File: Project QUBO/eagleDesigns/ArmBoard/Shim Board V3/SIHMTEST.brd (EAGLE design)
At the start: 79 x 69 mm, 30 parts, among them IC1 MCP2551/SN, U1 BME280

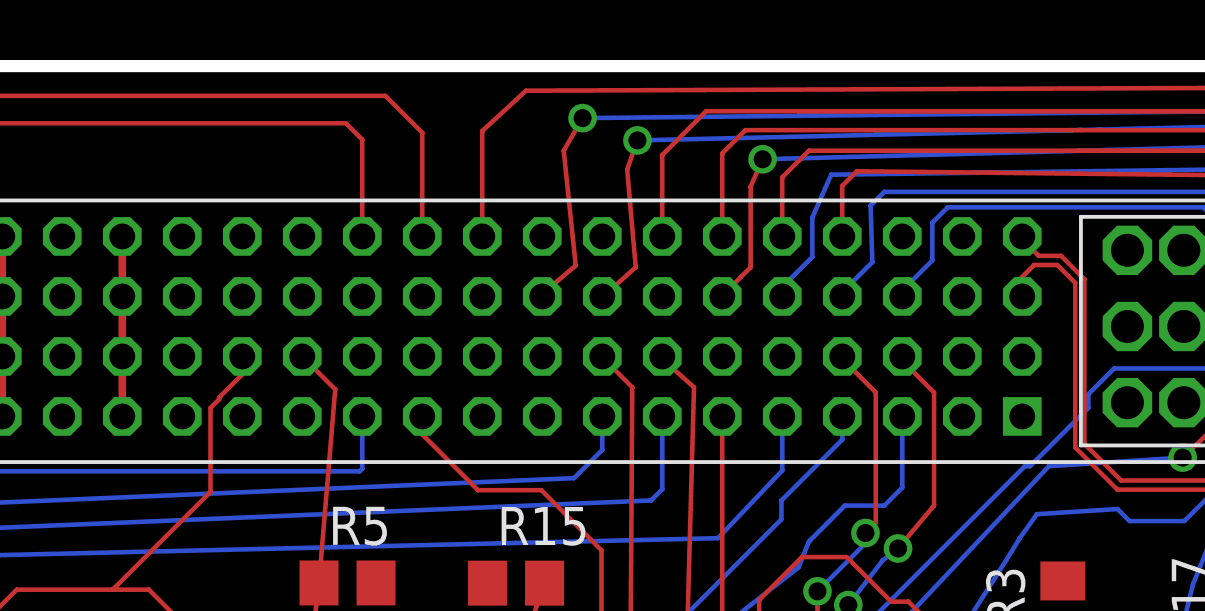
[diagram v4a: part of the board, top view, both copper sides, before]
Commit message: 
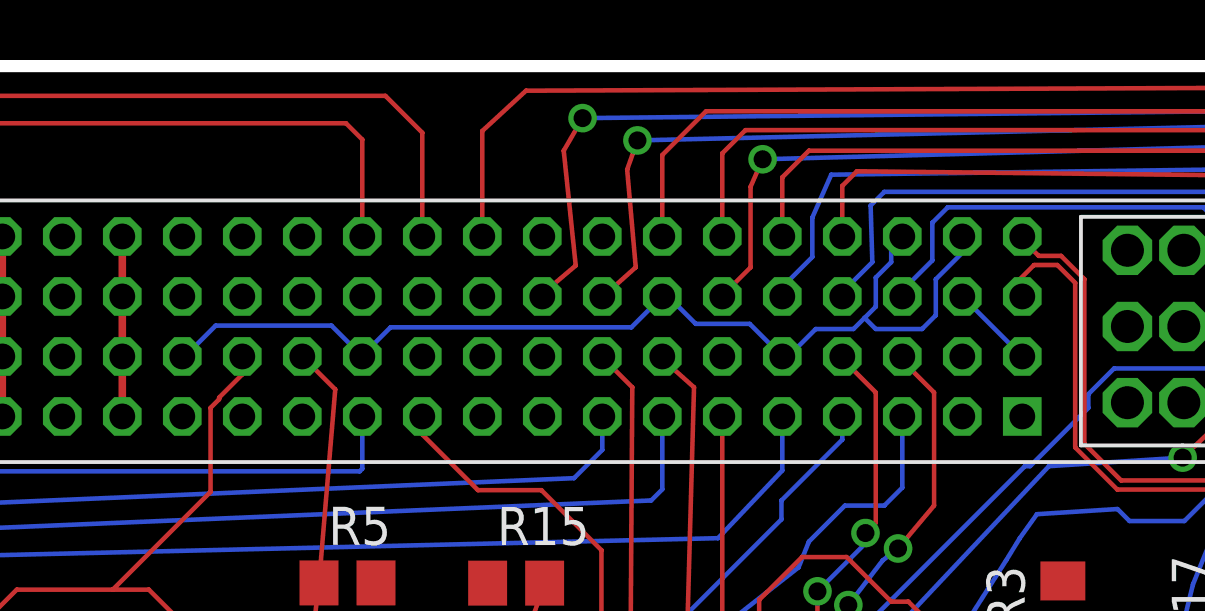
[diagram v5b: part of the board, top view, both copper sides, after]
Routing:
- net DGND: track 35.3 -> 72.8 mm
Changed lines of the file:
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@@
 <wire x1="70.58025" y1="43.94835" x2="64.7446" y2="43.94835" width="0.1524" layer="1"/>
 <wire x1="64.7446" y1="43.94835" x2="64.73825" y2="43.942" width="0.1524" layer="1"/>
-<wire x1="56.2049" y1="63.32125" x2="54.2049" y2="63.32125" width="0" layer="19" extent="1-1"/>
-<wire x1="58.2049" y1="59.32125" x2="56.2049" y2="61.32125" width="0" layer="19" extent="1-1"/>
-<wire x1="50.2049" y1="59.32125" x2="54.2049" y2="63.32125" width="0" layer="19" extent="1-1"/>
-<wire x1="46.2049" y1="61.32125" x2="50.2049" y2="59.32125" width="0" layer="19" extent="1-1"/>
-<wire x1="36.2049" y1="59.32125" x2="46.2049" y2="61.32125" width="0" layer="19" extent="1-1"/>
-<wire x1="30.2049" y1="59.32125" x2="36.2049" y2="59.32125" width="0" layer="19" extent="1-1"/>
+<wire x1="30.2049" y1="59.32125" x2="30.28905" y2="59.32125" width="0.1524" layer="16"/>
+<wire x1="30.28905" y1="59.32125" x2="31.3182" y2="60.3504" width="0.1524" layer="16"/>
+<wire x1="31.3182" y1="60.3504" x2="35.17575" y2="60.3504" width="0.1524" layer="16"/>
+<wire x1="35.17575" y1="60.3504" x2="36.2049" y2="59.32125" width="0.1524" layer="16"/>
+<wire x1="36.2049" y1="59.32125" x2="36.2049" y2="59.35065" width="0.1524" layer="16"/>
+<wire x1="36.2049" y1="59.35065" x2="37.1475" y2="60.29325" width="0.1524" layer="16"/>
+<wire x1="37.1475" y1="60.29325" x2="45.1769" y2="60.29325" width="0.1524" layer="16"/>
+<wire x1="45.1769" y1="60.29325" x2="46.2049" y2="61.32125" width="0.1524" layer="16"/>
+<wire x1="46.2049" y1="61.32125" x2="46.4065" y2="61.32125" width="0.1524" layer="16"/>
+<wire x1="46.4065" y1="61.32125" x2="47.3202" y2="60.40755" width="0.1524" layer="16"/>
+<wire x1="47.3202" y1="60.40755" x2="49.1186" y2="60.40755" width="0.1524" layer="16"/>
+<wire x1="49.1186" y1="60.40755" x2="50.2049" y2="59.32125" width="0.1524" layer="16"/>
+<wire x1="50.2049" y1="59.32125" x2="50.40585" y2="59.32125" width="0.1524" layer="16"/>
+<wire x1="50.40585" y1="59.32125" x2="51.3207" y2="60.2361" width="0.1524" layer="16"/>
+<wire x1="51.3207" y1="60.2361" x2="52.578" y2="60.2361" width="0.1524" layer="16"/>
+<wire x1="52.949475" y1="60.607575" x2="52.578" y2="60.2361" width="0.1524" layer="16"/>
+<wire x1="52.949475" y1="60.607575" x2="53.32095" y2="60.97905" width="0.1524" layer="16"/>
+<wire x1="53.32095" y1="60.97905" x2="53.32095" y2="61.9506" width="0.1524" layer="16"/>
+<wire x1="53.32095" y1="61.9506" x2="53.8353" y2="62.46495" width="0.1524" layer="16"/>
+<wire x1="53.8353" y1="62.46495" x2="53.8353" y2="62.95165" width="0.1524" layer="16"/>
+<wire x1="53.8353" y1="62.95165" x2="54.2049" y2="63.32125" width="0.1524" layer="16"/>
+<wire x1="56.2049" y1="61.32125" x2="58.2049" y2="59.32125" width="0.1524" layer="16"/>
+<wire x1="56.2049" y1="63.32125" x2="56.2049" y2="62.77715" width="0.1524" layer="16"/>
+<wire x1="56.2049" y1="62.77715" x2="55.3212" y2="61.89345" width="0.1524" layer="16"/>
+<wire x1="55.3212" y1="61.89345" x2="55.3212" y2="60.6933" width="0.1524" layer="16"/>
+<wire x1="55.3212" y1="60.6933" x2="54.864" y2="60.2361" width="0.1524" layer="16"/>
+<wire x1="54.864" y1="60.2361" x2="53.32095" y2="60.2361" width="0.1524" layer="16"/>
+<wire x1="53.32095" y1="60.2361" x2="52.949475" y2="60.607575" width="0.1524" layer="16"/>
 </signal>
 <signal name="RX_PF">
